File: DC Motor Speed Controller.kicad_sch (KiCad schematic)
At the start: 15 parts, among them J1 Screw_Terminal_01x02, J2 Screw_Terminal_01x02, Q1 TIP122, U1 NE555P

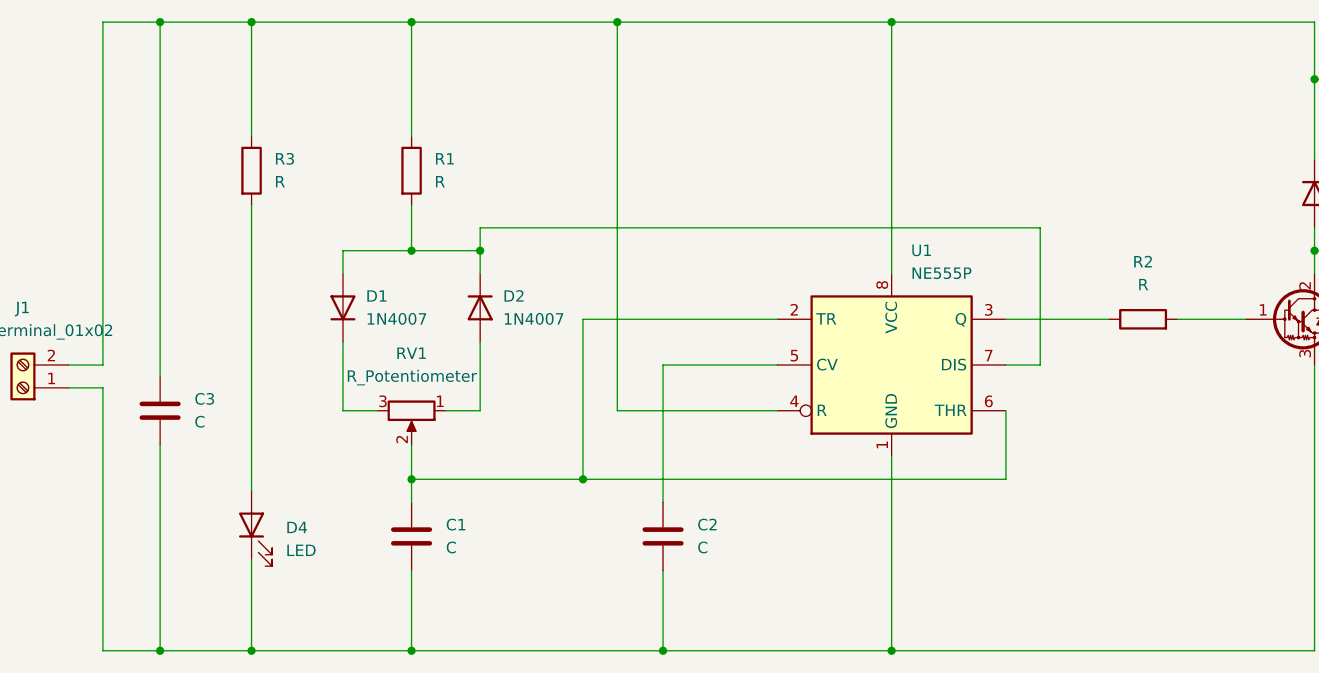
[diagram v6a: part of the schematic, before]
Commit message: Values to Components
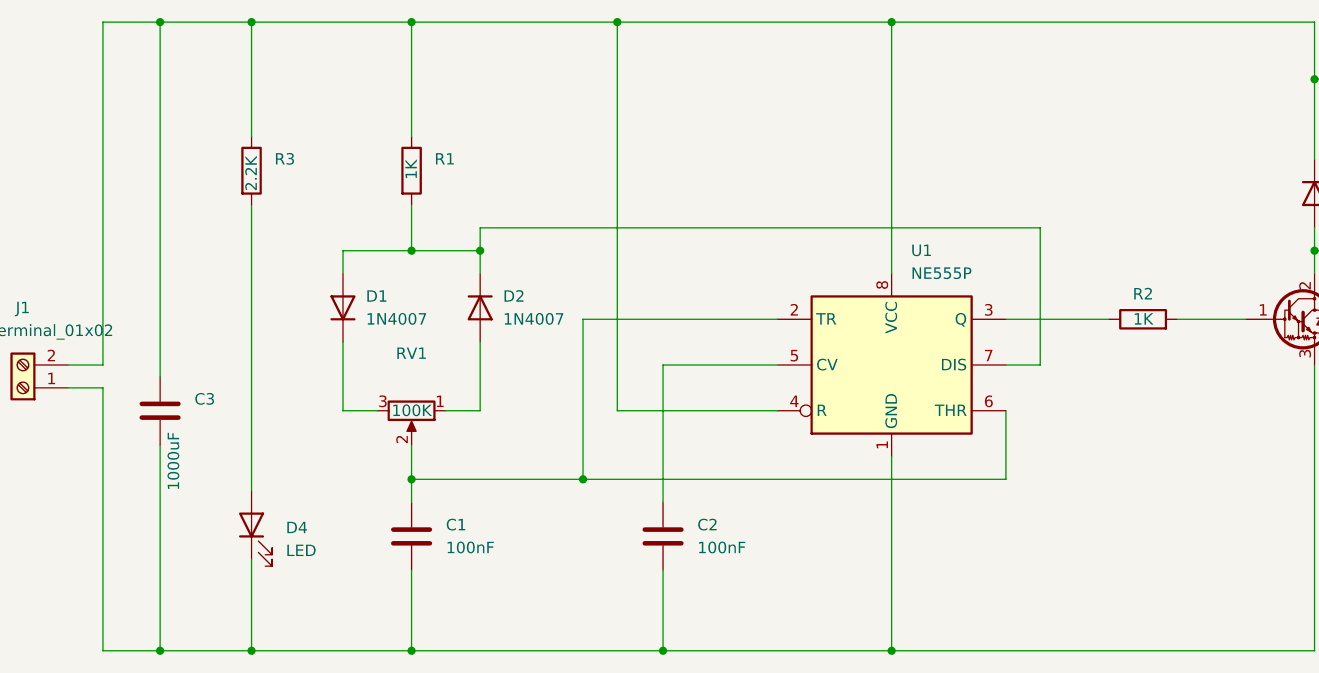
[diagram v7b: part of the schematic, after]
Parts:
- C1, C2: value C -> 100nF
- C3: value C -> 1000uF
- R1, R2: value R -> 1K
- R3: value R -> 2.2K
- RV1: value R_Potentiometer -> 100K
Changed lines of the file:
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@@
 		(on_board yes)
 		(dnp no)
-		(fields_autoplaced yes)
 		(property "Reference" "RV1"
 			(at 90.17 93.98 90)
@@
 			)
 		)
-		(property "Value" "R_Potentiometer"
-			(at 90.17 96.52 90)
+		(property "Value" "100K"
+			(at 90.17 100.33 90)
 			(effects
 				(font
@@
 		(on_board yes)
 		(dnp no)
-		(fields_autoplaced yes)
 		(property "Reference" "C3"
 			(at 66.04 99.0599 0)
@@
 			)
 		)
-		(property "Value" "C"
-			(at 66.04 101.5999 0)
+		(property "Value" "1000uF"
+			(at 63.754 109.22 90)
 			(effects
 				(font
@@
 		(on_board yes)
 		(dnp no)
-		(fields_autoplaced yes)
 		(property "Reference" "R2"
-			(at 171.45 83.82 90)
-			(effects
-				(font
-					(size 1.27 1.27)
-				)
-			)
-		)
-		(property "Value" "R"
-			(at 171.45 86.36 90)
+			(at 171.45 87.376 90)
+			(effects
+				(font
+					(size 1.27 1.27)
+				)
+			)
+		)
+		(property "Value" "1K"
+			(at 171.45 90.17 90)
 			(effects
 				(font
@@
 			)
 		)
-		(property "Value" "C"
+		(property "Value" "100nF"
 			(at 93.98 115.5699 0)
 			(effects
@@
 			)
 		)
-		(property "Value" "C"
+		(property "Value" "100nF"
 			(at 121.92 115.5699 0)
 			(effects
@@
 		(on_board yes)
 		(dnp no)
-		(fields_autoplaced yes)
 		(property "Reference" "R1"
 			(at 92.71 72.3899 0)
@@
 			)
 		)
-		(property "Value" "R"
-			(at 92.71 74.9299 0)
+		(property "Value" "1K"
+			(at 90.17 74.676 90)
 			(effects
 				(font
@@
 		(on_board yes)
 		(dnp no)
-		(fields_autoplaced yes)
 		(property "Reference" "R3"
 			(at 74.93 72.3899 0)
@@
 			)
 		)
-		(property "Value" "R"
-			(at 74.93 74.9299 0)
-			(effects
-				(font
+		(property "Value" "2.2K"
+			(at 72.39 75.946 90)
+			(effects
+				(font

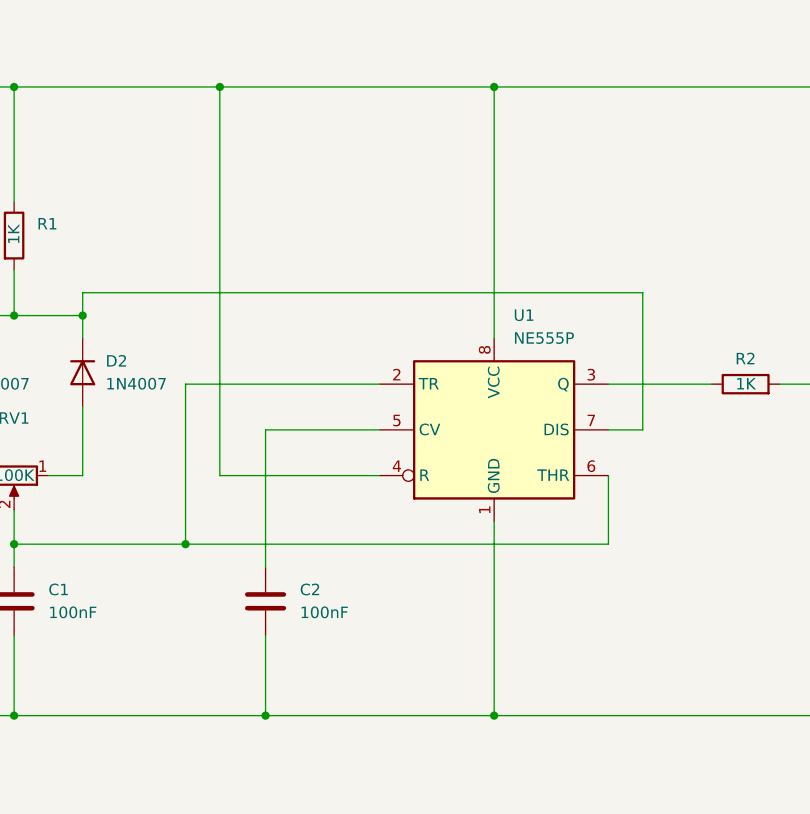
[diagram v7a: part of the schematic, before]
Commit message: Added GND and PWR
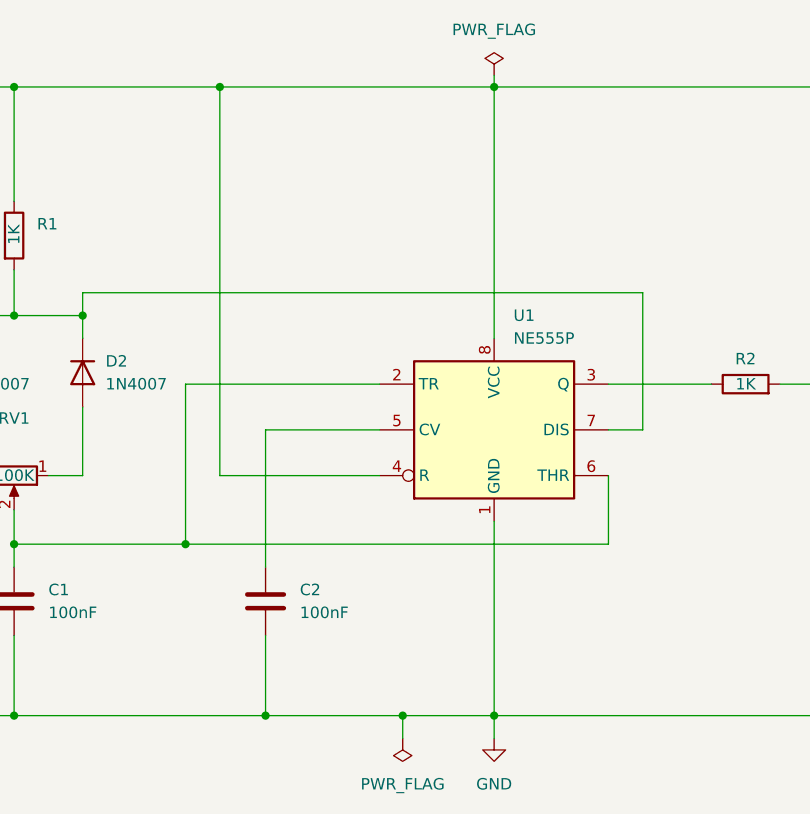
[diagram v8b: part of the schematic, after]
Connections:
- net GND: now reaches C1.2, C2.2, C3.2, D4.1 (K), J1.1 (Pin_1), Q1.3 (E), U1.1 (GND)
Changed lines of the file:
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@@
+	)
+	(junction
+		(at 133.35 127)
+		(diameter 0)
+		(color 0 0 0 0)
 	)
 	(junction
@@
 	(wire
 		(pts
+			(xy 143.51 127) (xy 143.51 129.54)
+		)
+		(stroke
+			(width 0)
+			(type default)
+		)
+	)
+	(wire
+		(pts
+			(xy 143.51 55.88) (xy 143.51 57.15)
+		)
+		(stroke
+			(width 0)
+			(type default)
+		)
+	)
+	(wire
+		(pts
 			(xy 62.23 96.52) (xy 62.23 57.15)
 		)
@@
 	(wire
 		(pts
+			(xy 133.35 127) (xy 143.51 127)
+		)
+		(stroke
+			(width 0)
+			(type default)
+		)
+	)
+	(wire
+		(pts
 			(xy 205.74 77.47) (xy 203.2 77.47)
 		)
@@
 	(wire
 		(pts
+			(xy 133.35 127) (xy 133.35 129.54)
+		)
+		(stroke
+			(width 0)
+			(type default)
+		)
+	)
+	(wire
+		(pts
 			(xy 82.55 92.71) (xy 82.55 100.33)
 		)
@@
 	(wire
 		(pts
-			(xy 118.11 127) (xy 143.51 127)
+			(xy 118.11 127) (xy 133.35 127)
 		)
 		(stroke
@@
 	)
 	(symbol
+		(lib_id "power:PWR_FLAG")
+		(at 143.51 55.88 0)
+		(unit 1)
+		(exclude_from_sim no)
+		(in_bom yes)
+		(on_board yes)
+		(dnp no)
+		(fields_autoplaced yes)
+		(property "Reference" "#FLG02"
+			(at 143.51 53.975 0)
+			(effects
+				(font
+					(size 1.27 1.27)
+				)
+				(hide yes)
+			)
+		)
+		(property "Value" "PWR_FLAG"
+			(at 143.51 50.8 0)
+			(effects
+				(font
+					(size 1.27 1.27)
+				)
+			)
+		)
+		(property "Footprint" ""
+			(at 143.51 55.88 0)
+			(effects
+				(font
+					(size 1.27 1.27)
+				)
+				(hide yes)
+			)
+		)
+		(property "Datasheet" "~"
+			(at 143.51 55.88 0)
+			(effects
+				(font
+					(size 1.27 1.27)
+				)
+				(hide yes)
+			)
+		)
+		(property "Description" "Special symbol for telling ERC where power comes from"
+			(at 143.51 55.88 0)
+			(effects
+				(font
+					(size 1.27 1.27)
+				)
+				(hide yes)
+			)
+		)
+		(pin "1"
+		)
+		(instances
+			(project ""
+				(path "/f6006c76-6b8e-4b9c-acef-dbdcf88c8838"
+					(reference "#FLG02")
+					(unit 1)
+				)
+			)
+		)
+	)
+	(symbol
 		(lib_id "Device:C")
 		(at 62.23 100.33 0)
@@
 	)
 	(symbol
+		(lib_id "power:PWR_FLAG")
+		(at 133.35 129.54 180)
+		(unit 1)
+		(exclude_from_sim no)
+		(in_bom yes)
+		(on_board yes)
+		(dnp no)
+		(fields_autoplaced yes)
+		(property "Reference" "#FLG01"
+			(at 133.35 131.445 0)
+			(effects
+				(font
+					(size 1.27 1.27)
+				)
+				(hide yes)
+			)
+		)
+		(property "Value" "PWR_FLAG"
+			(at 133.35 134.62 0)
+			(effects
+				(font
+					(size 1.27 1.27)
+				)
+			)
+		)
+		(property "Footprint" ""
+			(at 133.35 129.54 0)
+			(effects
+				(font
+					(size 1.27 1.27)
+				)
+				(hide yes)
+			)
+		)
+		(property "Datasheet" "~"
+			(at 133.35 129.54 0)
+			(effects
+				(font
+					(size 1.27 1.27)
+				)
+				(hide yes)
+			)
+		)
+		(property "Description" "Special symbol for telling ERC where power comes from"
+			(at 133.35 129.54 0)
+			(effects
+				(font
+					(size 1.27 1.27)
+				)
+				(hide yes)
+			)
+		)
+		(pin "1"
+		)
+		(instances
+			(project ""
+				(path "/f6006c76-6b8e-4b9c-acef-dbdcf88c8838"
+					(reference "#FLG01")
+					(unit 1)
+				)
+			)
+		)
+	)
+	(symbol
 		(lib_id "Connector:Screw_Terminal_01x02")
 		(at 210.82 74.93 0)
@@
 					(unit 1)
 				)
+			)
+		)
+	)
+	(symbol
+		(lib_id "power:GND")
+		(at 143.51 129.54 0)
+		(unit 1)
+		(exclude_from_sim no)
+		(in_bom yes)
+		(on_board yes)
+		(dnp no)
+		(fields_autoplaced yes)
+		(property "Reference" "#PWR01"
+			(at 143.51 135.89 0)
+			(effects
+				(font
+					(size 1.27 1.27)
+				)
+				(hide yes)
+			)
+		)
+		(property "Value" "GND"
+			(at 143.51 134.62 0)
+			(effects
+				(font
+					(size 1.27 1.27)
+				)
+			)
+		)
+		(property "Footprint" ""
+			(at 143.51 129.54 0)
+			(effects
+				(font
+					(size 1.27 1.27)
+				)
+				(hide yes)
+			)
+		)
+		(property "Datasheet" ""
+			(at 143.51 129.54 0)
+			(effects
+				(font
+					(size 1.27 1.27)
+				)
+				(hide yes)
+			)
+		)
+		(property "Description" "Power symbol creates a global label with name \"GND\" , ground"
+			(at 143.51 129.54 0)
+			(effects
+				(font
+					(size 1.27 1.27)
+				)
+				(hide yes)
+			)
+		)
+		(pin "1"
+		)
+		(instances
+			(project ""
+				(path "/f6006c76-6b8e-4b9c-acef-dbdcf88c8838"
+					(reference "#PWR01")
+					(unit 1)
+				)
